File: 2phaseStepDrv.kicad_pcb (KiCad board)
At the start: 2 copper layers, 12 parts, among them J1 Screw_Terminal_01x06, J2 Screw_Terminal_01x02, J3 Screw_Terminal_01x02, J4 Jack-DC, Q1 FMB2227A, Q2 FMB2227A, Q3 FMB2227A, Q4 FMB2227A, U1 4028

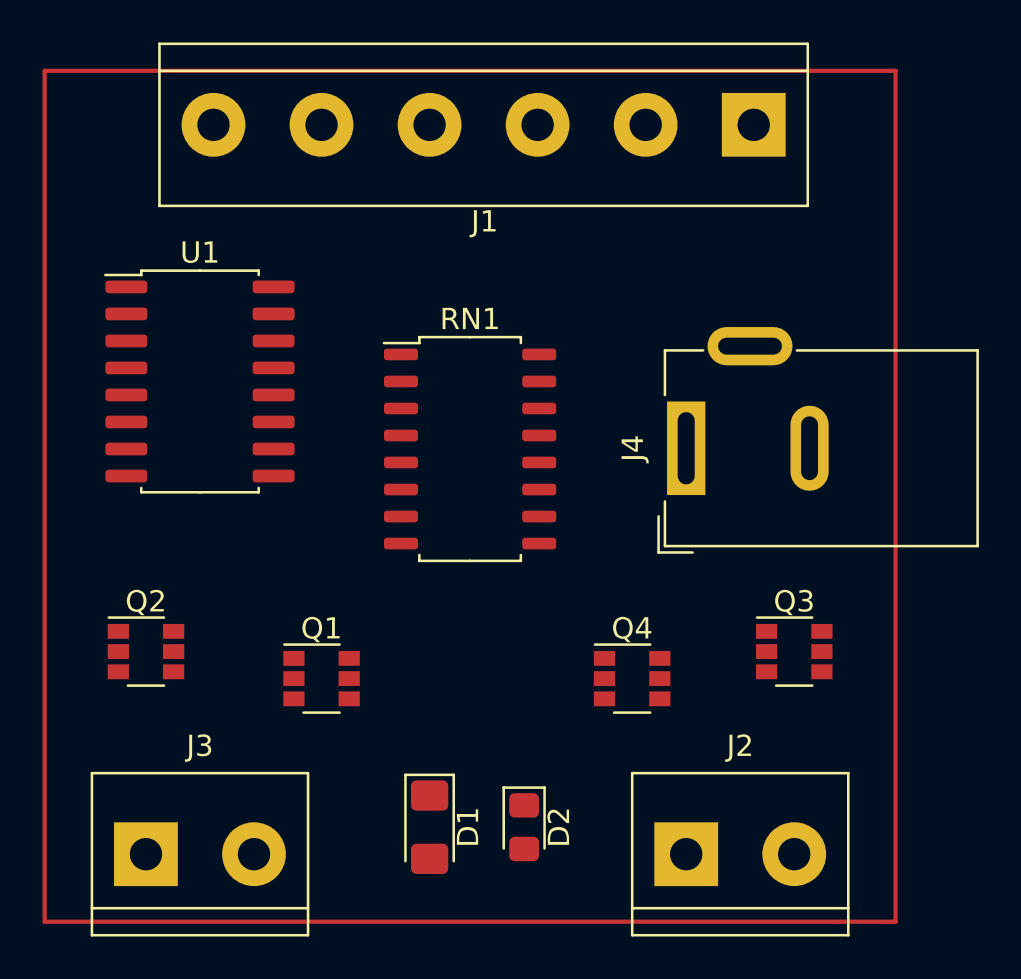
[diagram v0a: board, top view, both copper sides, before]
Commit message: Updated transistors, added flybacks and adjusted foor-prints
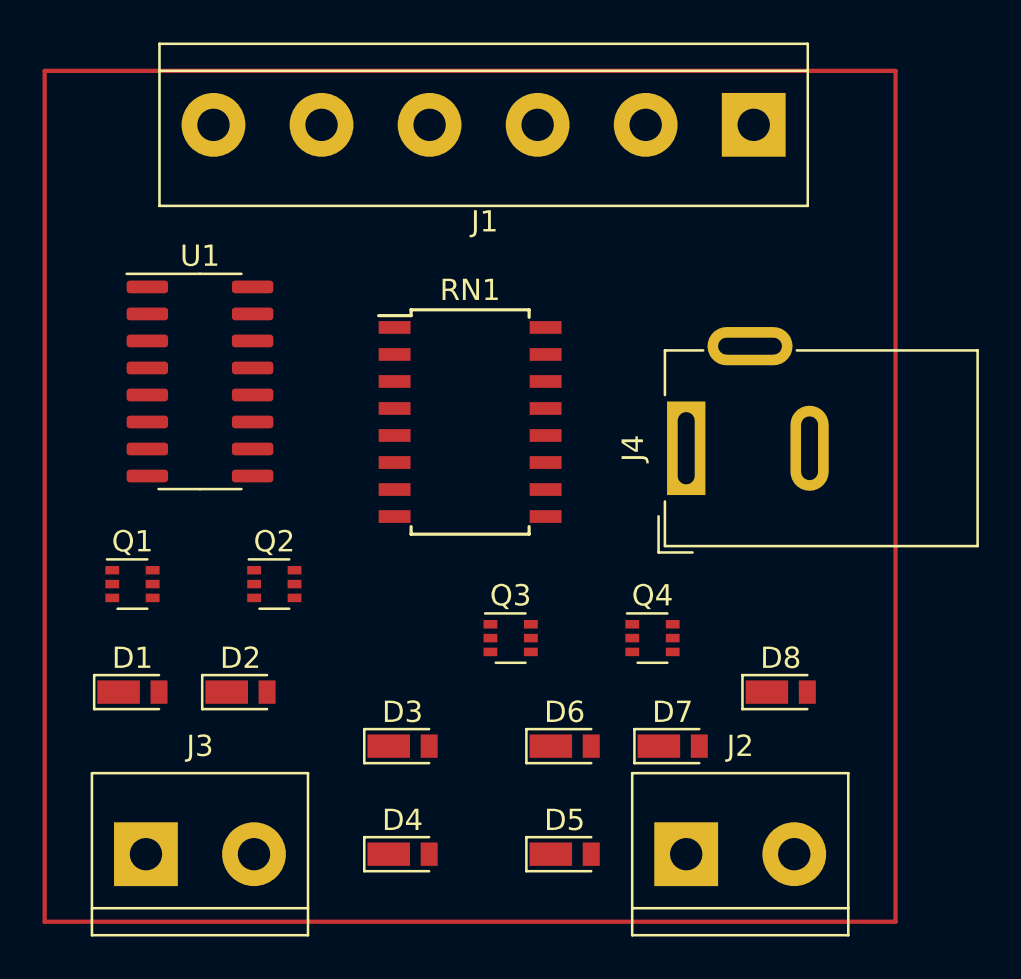
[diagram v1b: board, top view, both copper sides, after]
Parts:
- added D3: 1N4149, Diode_SMD:D_TUMD2, F.Cu at (96.5, 101.6)
- added D4: 1N4149, Diode_SMD:D_TUMD2, F.Cu at (96.5, 106.7)
- added D5: 1N4149, Diode_SMD:D_TUMD2, F.Cu at (104.1, 106.7)
- added D6: 1N4149, Diode_SMD:D_TUMD2, F.Cu at (104.1, 101.6)
- added D7: 1N4149, Diode_SMD:D_TUMD2, F.Cu at (109.2, 101.6)
- added D8: 1N4149, Diode_SMD:D_TUMD2, F.Cu at (114.3, 99.1)
- D1: footprint Diode_SMD:D_1206_3216Metric_Pad1.42x1.75mm_HandSolder -> Diode_SMD:D_TUMD2
- D2: footprint Diode_SMD:D_0805_2012Metric_Pad1.15x1.40mm_HandSolder -> Diode_SMD:D_TUMD2
- Q1, Q2, Q3, Q4: value FMB2227A -> MBT2222ADW1T1; footprint Package_TO_SOT_SMD:SuperSOT-6 -> Package_TO_SOT_SMD:SOT-363_SC-70-6
- RN1: footprint Package_SO:SOIC-16_4.55x10.3mm_P1.27mm -> Package_SO:SOIC-16W_5.3x10.2mm_P1.27mm
- U1: footprint Package_SO:SO-16_5.3x10.2mm_P1.27mm -> Package_SO:SOIC-16_3.9x9.9mm_P1.27mm
- moved D1 15.3 mm to (83.8, 99.1), turned to 0 degrees
- moved D2 14.8 mm to (88.9, 99.1), turned to 0 degrees
- moved Q3 13.4 mm to (101.6, 96.5)
- moved Q1 9.94 mm to (83.8, 94.0)
- moved Q2 6.82 mm to (90.5, 94.0)
- moved Q4 2.13 mm to (108.3, 96.5)
- moved RN1 1.27 mm to (99.7, 86.4)
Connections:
- D1 pad 2: Net-(J3-Pad1) -> Net-(D1-Pad2)
- D2 pad 1: Net-(J3-Pad1) -> Net-(D1-Pad2)
- J3 pad 1: Net-(J3-Pad1) -> Net-(D1-Pad2)
- Q1 pad 1: Net-(RN1-Pad8) -> Earth
- Q1 pad 2: Earth -> Net-(RN1-Pad7)
- Q1 pad 3: Net-(RN1-Pad7) -> +12V
- Q1 pad 4: Net-(J3-Pad2) -> Net-(D1-Pad2)
- Q1 pad 5: Net-(J3-Pad1) -> Net-(RN1-Pad8)
- Q1 pad 6: +12V -> Net-(J3-Pad2)
- Q2 pad 1: Net-(RN1-Pad6) -> Earth
- Q2 pad 2: Earth -> Net-(RN1-Pad5)
- Q2 pad 3: Net-(RN1-Pad5) -> +12V
- Q2 pad 4: Net-(J3-Pad1) -> Net-(J3-Pad2)
- Q2 pad 5: Net-(J3-Pad2) -> Net-(RN1-Pad6)
- Q2 pad 6: +12V -> Net-(D1-Pad2)
- Q3 pad 1: Net-(RN1-Pad4) -> Earth
- Q3 pad 2: Earth -> Net-(RN1-Pad3)
- Q3 pad 3: Net-(RN1-Pad3) -> +12V
- Q3 pad 4: Net-(J2-Pad2) -> Net-(J2-Pad1)
- Q3 pad 5: Net-(J2-Pad1) -> Net-(RN1-Pad4)
- Q3 pad 6: +12V -> Net-(J2-Pad2)
- Q4 pad 1: Net-(RN1-Pad2) -> Earth
- Q4 pad 2: Earth -> Net-(RN1-Pad1)
- Q4 pad 3: Net-(RN1-Pad1) -> +12V
- Q4 pad 4: Net-(J2-Pad1) -> Net-(J2-Pad2)
- Q4 pad 5: Net-(J2-Pad2) -> Net-(RN1-Pad2)
- Q4 pad 6: +12V -> Net-(J2-Pad1)
